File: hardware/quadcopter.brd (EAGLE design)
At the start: 132 x 132 mm, 63 parts, among them J1 AVR_SPI_PRG_6NS, J3 HEADER-10POSTH-254X10, J4 HEADER-4POS-0.1IN-FEMALE-SMD-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, J6 HEADER-4POS-0.1IN-FEMALE, Q3 MOSFET-FET-SI2302CDS-T1-E3CT-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, Q4 MOSFET-FET-SI2302CDS-T1-E3CT-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, Q5 MOSFET-FET-SI2302CDS-T1-E3CT-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, Q6 MOSFET-FET-SI2302CDS-T1-E3CT-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, U1 ATMEGA128RFA1, U2 IMU-LSM6DSOXTR-497-18367-1-ND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

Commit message: fixing many issues from quick check
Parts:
- moved C18 4.12 mm to (-22.0, -24.0)
- moved R1 0.41 mm to (-15.0, 27.0)
- renumbered LED_1 to L1, LED_2 to L2, LED_3 to L3, LED_4 to L4, NETBRIDGE to NB, VOLTAGE_REGULATOR1 to VR1
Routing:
- net BAT_GND: track 60.6 -> 51.5 mm
- net RESET: track 122.4 -> 122.9 mm

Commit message: fixing many issues from quick check
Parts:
- renumbered MOTOR_PAD_1 to MP1, MOTOR_PAD_2 to MP2, MOTOR_PAD_3 to MP3, MOTOR_PAD_4 to MP4
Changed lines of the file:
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@@
 </text>
 <text x="7" y="-32" size="0.8128" layer="21" font="vector">3V  GND  SCL  SDA</text>
+<dimension x1="-53.36431875" y1="62.99101875" x2="-61.99101875" y2="54.36431875" x3="-51" y3="52" textsize="1.778" layer="48" dtype="diameter"/>
+<dimension x1="-57.677671875" y1="58.677671875" x2="-65.959840625" y2="58.1339375" x3="-73.743084375" y3="57.622959375" textsize="1.778" layer="48" dtype="radius"/>
+<dimension x1="-40" y1="27.190959375" x2="-40" y2="-25.190959375" x3="-59" y3="1" textsize="1.778" layer="48"/>
+<dimension x1="26.190959375" y1="41" x2="-26.190959375" y2="41" x3="0" y3="48" textsize="1.778" layer="48"/>
 </plain>
 <attributes>
@@
 <attribute name="MOUNTING" value="SMD" x="48" y="-69.5" size="1.778" layer="27" display="off"/>
 <attribute name="MPN" value="C2012X7R2A104K125AA" x="48" y="-69.5" size="1.778" layer="27" display="off"/>
-<attribute name="NAME" x="-14.23" y="-6" size="0.9" layer="25" font="vector"/>
+<attribute name="NAME" x="-15.23" y="-5" size="0.9" layer="25" font="vector"/>
 <attribute name="PACKAGE" value="0805" x="48" y="-69.5" size="1.778" layer="27" display="off"/>
 <attribute name="REVIEWER" value="Swanson" x="48" y="-69.5" size="1.778" layer="27" display="off"/>
@@
 <attribute name="VALUE" x="35" y="4.6191" size="1.27" layer="27" font="vector" align="top-center"/>
 </element>
-<element name="MOTOR_PAD_1" library="quadparts_prebuilt_2022" package="MOLEX-0532610271" value="MOTOR_PADS_GND-MOLEX-SMD" x="46" y="-43" smashed="yes">
+<element name="MP1" library="quadparts_prebuilt_2022" package="MOLEX-0532610271" value="MOTOR_PADS_GND-MOLEX-SMD" x="46" y="-43" smashed="yes">
 <attribute name="CREATOR" value="Swanson" x="76.48" y="-51.89" size="1.778" layer="27" display="off"/>
 <attribute name="DESC" value="CONN HEADER SMD R/A 2POS 1.25MM" x="76.48" y="-51.89" size="1.778" layer="27" display="off"/>
@@
 <attribute name="NAME" x="46" y="-38.1" size="0.9" layer="25" font="vector" align="center"/>
 </element>
-<element name="MOTOR_PAD_2" library="quadparts_prebuilt_2022" package="MOLEX-0532610271" value="MOTOR_PADS_GND-MOLEX-SMD" x="45" y="46" smashed="yes" rot="R180">
+<element name="MP2" library="quadparts_prebuilt_2022" package="MOLEX-0532610271" value="MOTOR_PADS_GND-MOLEX-SMD" x="45" y="46" smashed="yes" rot="R180">
 <attribute name="CREATOR" value="Swanson" x="4.36" y="54.89" size="1.778" layer="27" rot="R180" display="off"/>
 <attribute name="DESC" value="CONN HEADER SMD R/A 2POS 1.25MM" x="4.36" y="54.89" size="1.778" layer="27" rot="R180" display="off"/>
@@
 <attribute name="NAME" x="45" y="41.1" size="0.9" layer="25" font="vector" rot="R180" align="center"/>
 </element>
-<element name="MOTOR_PAD_3" library="quadparts_prebuilt_2022" package="MOLEX-0532610271" value="MOTOR_PADS_GND-MOLEX-SMD" x="-48" y="47" smashed="yes" rot="R180">
+<element name="MP3" library="quadparts_prebuilt_2022" package="MOLEX-0532610271" value="MOTOR_PADS_GND-MOLEX-SMD" x="-48" y="47" smashed="yes" rot="R180">
 <attribute name="CREATOR" value="Swanson" x="-98.8" y="55.89" size="1.778" layer="27" rot="R180" display="off"/>
 <attribute name="DESC" value="CONN HEADER SMD R/A 2POS 1.25MM" x="-98.8" y="55.89" size="1.778" layer="27" rot="R180" display="off"/>
@@
 <attribute name="NAME" x="-48" y="42.1" size="0.9" layer="25" font="vector" rot="R180" align="center"/>
 </element>
-<element name="MOTOR_PAD_4" library="quadparts_prebuilt_2022" package="MOLEX-0532610271" value="MOTOR_PADS_GND-MOLEX-SMD" x="-47" y="-44" smashed="yes">
+<element name="MP4" library="quadparts_prebuilt_2022" package="MOLEX-0532610271" value="MOTOR_PADS_GND-MOLEX-SMD" x="-47" y="-44" smashed="yes">
 <attribute name="CREATOR" value="Swanson" x="13.96" y="-52.89" size="1.778" layer="27" display="off"/>
 <attribute name="DESC" value="CONN HEADER SMD R/A 2POS 1.25MM" x="13.96" y="-52.89" size="1.778" layer="27" display="off"/>
@@
 <wire x1="3.00355" y1="-35.97275" x2="3" y2="-36" width="0.127" layer="1"/>
 <wire x1="7.8232" y1="-29.54655" x2="7.85" y2="-29.51" width="0.127" layer="1"/>
-<wire x1="-12.64285" y1="-18.51025" x2="-12.64285" y2="-20.5359" width="0.127" layer="1"/>
+<wire x1="-12.64285" y1="-20.5359" x2="-12.64285" y2="-18.51025" width="0.127" layer="1"/>
 <wire x1="-14.59865" y1="-16.55445" x2="-12.64285" y2="-18.51025" width="0.127" layer="1"/>
-<wire x1="-12.64285" y1="-20.5359" x2="-12.62" y2="-20.68" width="0.127" layer="1"/>
+<wire x1="-12.62" y1="-20.68" x2="-12.64285" y2="-20.5359" width="0.127" layer="1"/>
 <wire x1="-14.59865" y1="-16.55445" x2="-14.615" y2="-16.42" width="0.127" layer="1"/>
 <wire x1="-16.27505" y1="-11.38555" x2="-16.27505" y2="-6.0071" width="0.127" layer="16"/>
@@
 </signal>
 <signal name="VBAT" class="1">
-<contactref element="MOTOR_PAD_1" pad="1"/>
+<contactref element="MP1" pad="1"/>
 <contactref element="D5" pad="1"/>
-<contactref element="MOTOR_PAD_2" pad="1"/>
+<contactref element="MP2" pad="1"/>
 <contactref element="D6" pad="1"/>
-<contactref element="MOTOR_PAD_3" pad="1"/>
+<contactref element="MP3" pad="1"/>
 <contactref element="D7" pad="1"/>
-<contactref element="MOTOR_PAD_4" pad="1"/>
+<contactref element="MP4" pad="1"/>
 <contactref element="D8" pad="1"/>
 <contactref element="R13" pad="2"/>
@@
 <wire x1="44.525" y1="38" x2="45.49395" y2="38" width="0.3048" layer="1"/>
 <wire x1="37.525" y1="-28" x2="38.49395" y2="-28" width="0.3048" layer="1"/>
-<wire x1="-22.895" y1="-24" x2="-24.0594" y2="-24" width="0.3048" layer="1"/>
+<wire x1="-24.0594" y1="-24" x2="-22.895" y2="-24" width="0.3048" layer="1"/>
 <wire x1="-47.3625" y1="44.1" x2="-47.3625" y2="42.8456" width="0.3048" layer="1"/>
 <wire x1="-38.525" y1="-30" x2="-39.49395" y2="-30" width="0.3048" layer="1"/>
@@
 </signal>
 <signal name="BAT_GND">
-<contactref element="MOTOR_PAD_1" pad="G1"/>
-<contactref element="MOTOR_PAD_1" pad="G2"/>
-<contactref element="MOTOR_PAD_2" pad="G1"/>
-<contactref element="MOTOR_PAD_2" pad="G2"/>
+<contactref element="MP1" pad="G1"/>
+<contactref element="MP1" pad="G2"/>
+<contactref element="MP2" pad="G1"/>
+<contactref element="MP2" pad="G2"/>
 <contactref element="Q4" pad="S"/>
-<contactref element="MOTOR_PAD_3" pad="G1"/>
-<contactref element="MOTOR_PAD_3" pad="G2"/>
+<contactref element="MP3" pad="G1"/>
+<contactref element="MP3" pad="G2"/>
 <contactref element="Q5" pad="S"/>
-<contactref element="MOTOR_PAD_4" pad="G1"/>
-<contactref element="MOTOR_PAD_4" pad="G2"/>
+<contactref element="MP4" pad="G1"/>
+<contactref element="MP4" pad="G2"/>
 <contactref element="Q6" pad="S"/>
 <contactref element="R7" pad="1"/>
@@
 </polygon>
 <wire x1="38.95" y1="-37.15" x2="38.95" y2="-38.3544" width="0.3048" layer="1"/>
-<wire x1="-23.5" y1="-31.25" x2="-23.5" y2="-29.5456" width="0.3048" layer="1"/>
+<wire x1="-23.5" y1="-29.5456" x2="-23.5" y2="-31.25" width="0.3048" layer="1"/>
 <wire x1="26.66" y1="-25" x2="25.3379" y2="-25" width="0.3048" layer="1"/>
 <wire x1="-25.955" y1="21" x2="-27.0994" y2="21" width="0.3048" layer="1"/>
@@
 <wire x1="-19.8374" y1="-23.8887" x2="-17.6022" y2="-21.6535" width="0.127" layer="1"/>
 <wire x1="-15.2273" y1="-21.6535" x2="-15.22" y2="-21.63" width="0.127" layer="1"/>
-<wire x1="-19.8374" y1="-23.8887" x2="-19.9406" y2="-24" width="0.127" layer="1"/>
+<wire x1="-19.9406" y1="-24" x2="-19.8374" y2="-23.8887" width="0.127" layer="1"/>
 </signal>
 <signal name="PWM2">
@@
 <signal name="N$18" class="1">
 <contactref element="Q3" pad="D"/>
-<contactref element="MOTOR_PAD_1" pad="2"/>
+<contactref element="MP1" pad="2"/>
 <contactref element="D5" pad="2"/>
 <contactref element="C11" pad="1"/>
@@
 <signal name="N$19" class="1">
 <contactref element="Q4" pad="D"/>
-<contactref element="MOTOR_PAD_2" pad="2"/>
+<contactref element="MP2" pad="2"/>
 <contactref element="D6" pad="2"/>
 <wire x1="44.3875" y1="43.1" x2="44.3875" y2="40.9125" width="0.1524" layer="1"/>
@@
 <signal name="N$20" class="1">
 <contactref element="Q5" pad="D"/>
-<contactref element="MOTOR_PAD_3" pad="2"/>
+<contactref element="MP3" pad="2"/>
 <contactref element="D7" pad="2"/>
 <wire x1="-48.6125" y1="44.1" x2="-48.6125" y2="41.6125" width="0.1524" layer="1"/>
@@
 <signal name="N$21" class="1">
 <contactref element="Q6" pad="D"/>
-<contactref element="MOTOR_PAD_4" pad="2"/>
+<contactref element="MP4" pad="2"/>
 <contactref element="D8" pad="2"/>
-<wire x1="-33" y1="-35.125" x2="-42.125" y2="-35.125" width="0.3048" layer="1"/>
+<wire x1="-42.125" y1="-35.125" x2="-33" y2="-35.125" width="0.3048" layer="1"/>
 <wire x1="-42.125" y1="-35.125" x2="-46.3875" y2="-39.3875" width="0.3048" layer="1"/>
 <wire x1="-46.3875" y1="-39.3875" x2="-46.3875" y2="-41.1" width="0.3048" layer="1"/>
 <wire x1="-35.475" y1="-30" x2="-34" y2="-30" width="0.1524" layer="1"/>
 <wire x1="-34" y1="-30" x2="-33" y2="-31" width="0.1524" layer="1"/>
-<wire x1="-33" y1="-31" x2="-33" y2="-35.125" width="0.1524" layer="1"/>
+<wire x1="-33" y1="-35.125" x2="-33" y2="-31" width="0.1524" layer="1"/>
 </signal>
 <signal name="PWM1">

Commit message: ready for full check, fixed last few trivial issues
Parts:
- added U$1: (no value), quadparts_prebuilt_2022:LAYER_LABELS
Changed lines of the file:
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@@
 </text>
 <text x="7" y="-32" size="0.8128" layer="21" font="vector">3V  GND  SCL  SDA</text>
-<dimension x1="-53.36431875" y1="62.99101875" x2="-61.99101875" y2="54.36431875" x3="-51" y3="52" textsize="1.778" layer="48" dtype="diameter"/>
-<dimension x1="-57.677671875" y1="58.677671875" x2="-65.959840625" y2="58.1339375" x3="-73.743084375" y3="57.622959375" textsize="1.778" layer="48" dtype="radius"/>
-<dimension x1="-40" y1="27.190959375" x2="-40" y2="-25.190959375" x3="-59" y3="1" textsize="1.778" layer="48"/>
-<dimension x1="26.190959375" y1="41" x2="-26.190959375" y2="41" x3="0" y3="48" textsize="1.778" layer="48"/>
+<dimension x1="-53.36431875" y1="62.99101875" x2="-61.99101875" y2="54.36431875" x3="-51" y3="52" textsize="1.778" layer="47" dtype="diameter"/>
+<dimension x1="-57.677671875" y1="58.677671875" x2="-65.959840625" y2="58.1339375" x3="-73.743084375" y3="57.622959375" textsize="1.778" layer="47" dtype="radius"/>
+<dimension x1="-40" y1="27.190959375" x2="-40" y2="-25.190959375" x3="-59" y3="1" textsize="1.778" layer="47"/>
+<dimension x1="26.190959375" y1="41" x2="-26.190959375" y2="41" x3="0" y3="48" textsize="1.778" layer="47"/>
 </plain>
 <attributes>
@@
 <attribute name="VALUE" x="-36" y="0.5" size="0.9" layer="27" font="vector" align="center"/>
 </element>
+<element name="U$1" library="quadparts_prebuilt_2022" package="LAYER_LABELS" value="" x="-1" y="-41" smashed="yes">
+</element>
 </elements>

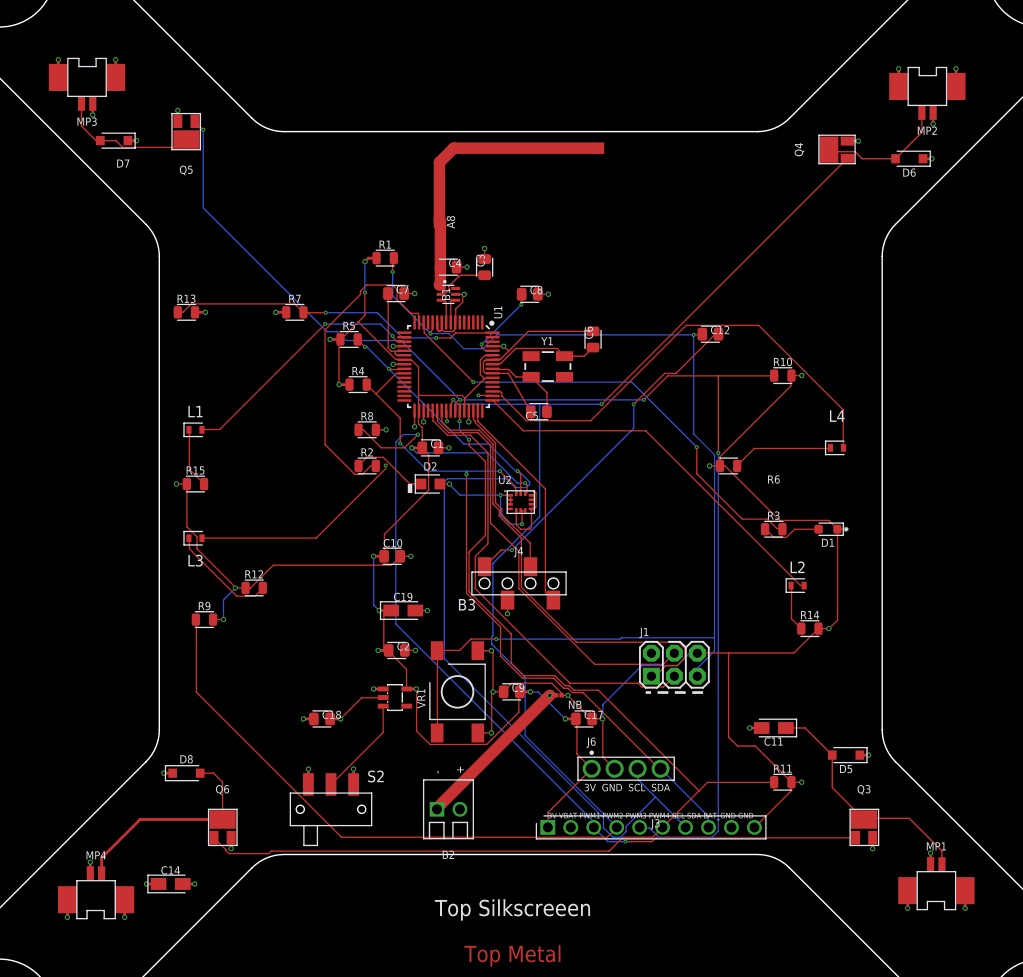
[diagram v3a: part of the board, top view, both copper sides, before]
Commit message: fixed a bunch of routing issues/vias, added logo
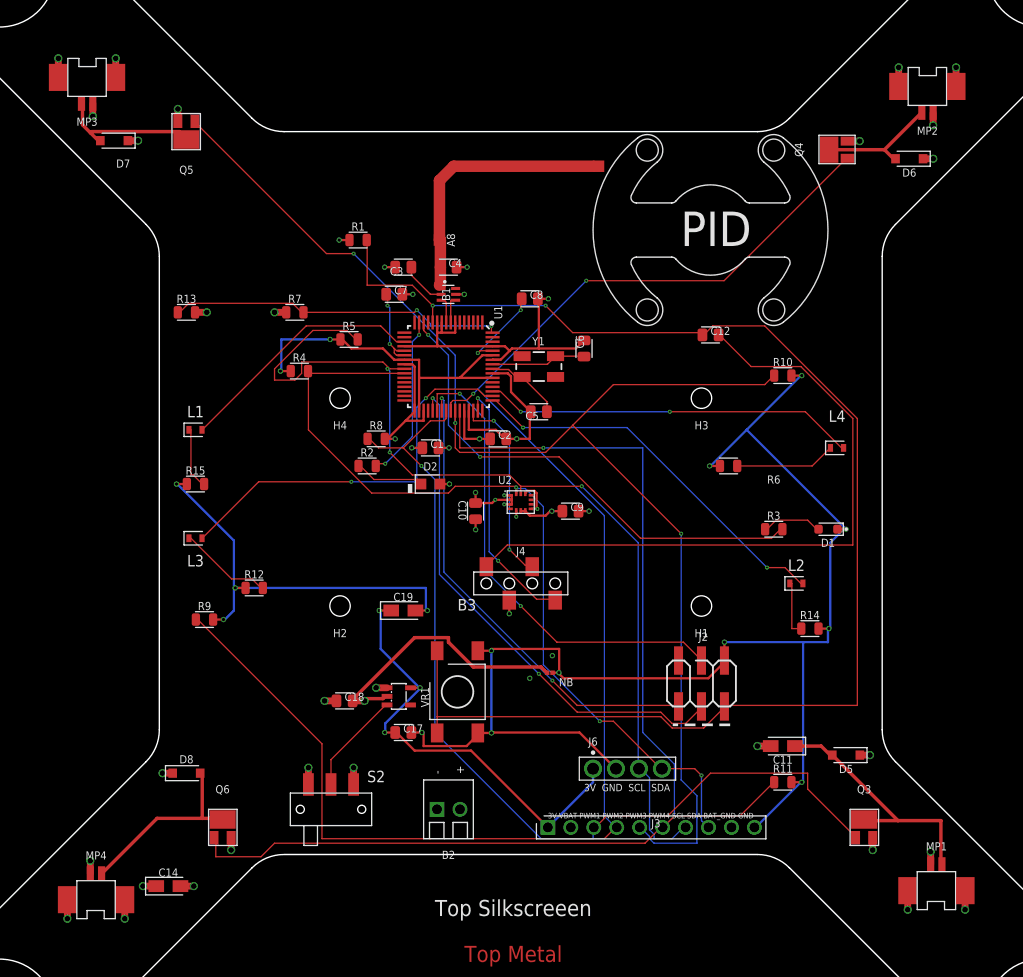
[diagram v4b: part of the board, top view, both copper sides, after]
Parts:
- removed J1: AVR_SPI_PRG_6NS, quadparts_prebuilt_2022:2X3-NS
- added H1, H2, H3, H4: MOUNTING_HOLE-2-56, quadparts_prebuilt_2022:2-56-MOUNTING-HOLE-NO-METAL
- added J2: AVR_SPI_PRG_6-SMD, quadparts_prebuilt_2022:2X3-SMD
- added U$2: PIDLOGO, logo:PIDLOGO
- moved C2 26.0 mm to (-2.50, 7.00)
- moved C9 21.0 mm to (5.50, -1.00)
- moved C17 20.1 mm to (-13.0, -25.5)
- moved C10 10.5 mm to (-5.00, -1.00), turned to 90.1 degrees
- moved C3 9.00 mm to (-13.0, 26.0), turned to 180 degrees
- moved R4 6.67 mm to (-24.5, 14.5)
- moved R1 3.61 mm to (-18.0, 29.0)
- moved C18 3.20 mm to (-19.5, -22.0)
- moved NB 2.69 mm to (3.22, -18.9)
- moved C11 2.24 mm to (29.0, -27.0)
- moved A8 2.00 mm to (-9.00, 29.0)
- moved C6 1.41 mm to (7.00, 17.0)
- moved R8 1.41 mm to (-16.0, 7.00)
- moved Y1 1.00 mm to (2.00, 15.0)
- moved C8 0.50 mm to (1.00, 22.5)
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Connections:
- net GND: now also J2.6; no longer J1.6
- net MISO: now also J2.1; no longer J1.1
- net MOSI: now also J2.4; no longer J1.4
- net RESET: now also J2.5; no longer J1.5
- net SCK: now also J2.3; no longer J1.3
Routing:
- net GND: track 241.6 -> 291.8 mm, vias 33 -> 29
- net 3V: track 154.6 -> 105.0 mm
- net N$13: track 38.1 -> 74.3 mm, vias 2 -> 0
- net RESET: track 122.9 -> 157.8 mm, vias 4 -> 2
- net PG1: track 35.6 -> 18.3 mm, vias 0 -> 2
- net SDA: track 81.3 -> 94.5 mm
- net LED4: track 52.8 -> 41.4 mm, vias 0 -> 2
- net PWM4: track 124.5 -> 135.8 mm, vias 2 -> 1
- net BAT_GND: track 51.5 -> 58.8 mm, vias 18 -> 17
- net MOSI: track 46.5 -> 53.2 mm, vias 0 -> 2
- net SCK: track 51.3 -> 57.9 mm, vias 0 -> 2
- net PWM1: track 97.4 -> 103.5 mm, vias 3 -> 1
- net SCL: track 103.0 -> 108.5 mm
- net LED3: track 39.0 -> 44.1 mm
- net PWM3: track 144.4 -> 149.4 mm, vias 4 -> 3
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
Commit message: fixed a bunch of routing issues/vias, added logo
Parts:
- renumbered U$2 to LOGO
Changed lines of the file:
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@@
 <attribute name="NAME" x="-20" y="8.5" size="0.9" layer="25" font="vector" align="center"/>
 </element>
-<element name="U$2" library="logo" package="PIDLOGO" value="PIDLOGO" x="21" y="39" smashed="yes">
+<element name="LOGO" library="logo" package="PIDLOGO" value="PIDLOGO" x="21" y="39" smashed="yes">
 </element>
 </elements>
